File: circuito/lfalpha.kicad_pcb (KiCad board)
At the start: 2 copper layers, 200 x 100 mm, 48 parts, among them J1 BAT, J2 ANALOG, J3 MotorA, J4 MotorB, J5 Bluetooth, J6 REMOTE S/S, J7 SPI, J8 SENSOR CON, J9 SENSOR BAR, SW1 ON/OFF, SW2 START, SW3 STOP, U1 AruinoNano, U2 DRV8835-Carrier, U3 QRE1113, U4 QRE1113, U5 QRE1113, U6 QRE1113, U7 QRE1113, U8 QRE1113

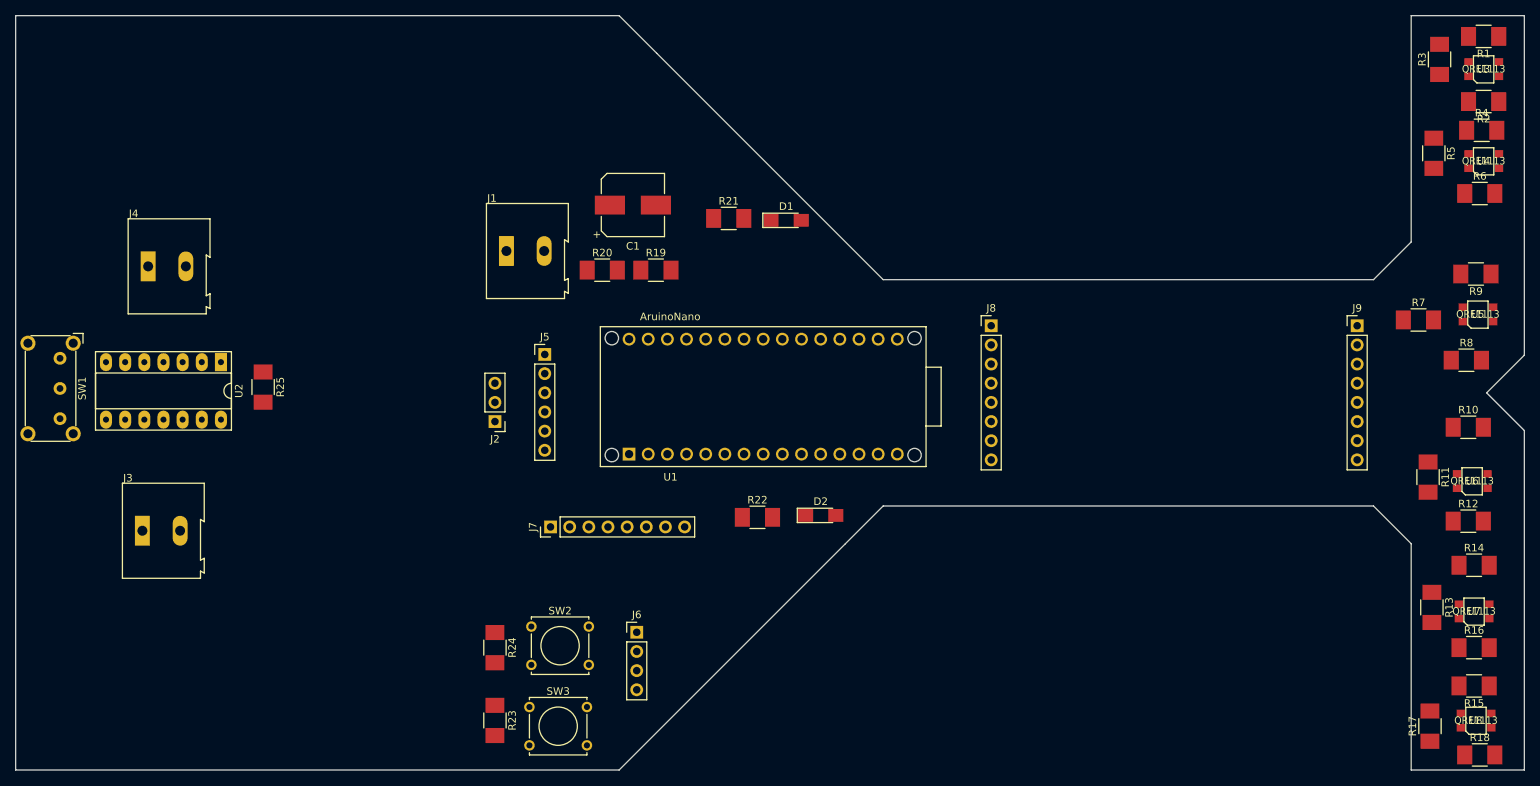
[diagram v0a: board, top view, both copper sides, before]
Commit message: Definito il layout del PCB definitivo
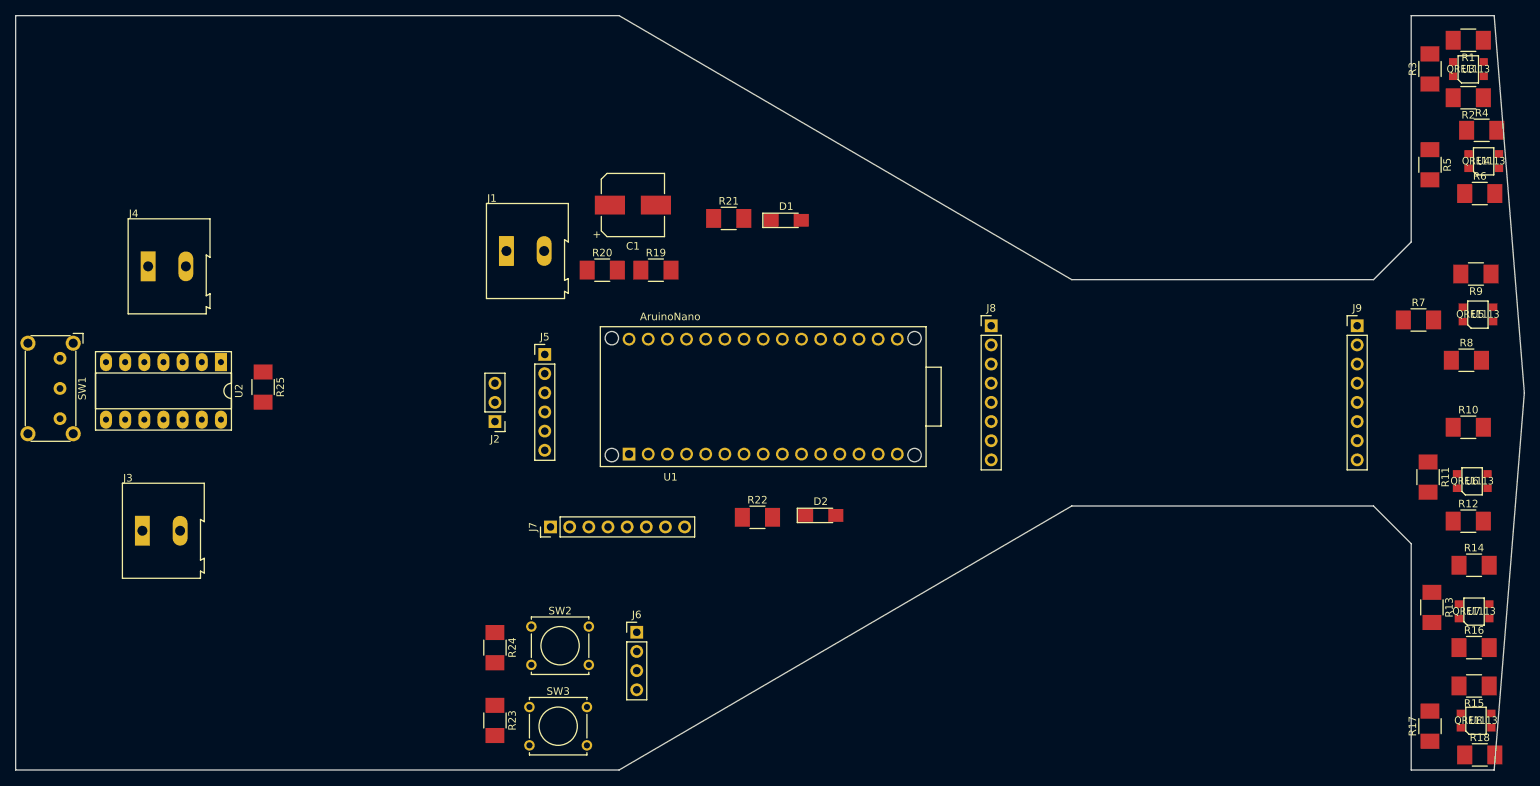
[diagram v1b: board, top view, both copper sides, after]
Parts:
- moved R1 2.09 mm to (242.6, 48.3)
- moved R2 2.09 mm to (242.6, 55.9)
- moved U3 2.03 mm to (242.6, 52.1)
- moved R3 1.80 mm to (237.5, 52.1)
- moved R5 1.61 mm to (237.5, 64.8)
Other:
- outline, holes or cut-outs redrawn
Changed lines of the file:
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@@
-(kicad_pcb (version 4) (host pcbnew 4.0.7-e0-6372~58~ubuntu14.04.1)
+(kicad_pcb (version 4) (host pcbnew 4.0.6)
   (general
     (links 125)
     (no_connects 125)
-    (area 40.455 44.377 250.075001 146.477)
+    (area 40.455 44.885 250.075001 146.477)
     (thickness 1.6)
-    (drawings 19)
+    (drawings 15)
     (tracks 0)
     (zones 0)
@@
   )
   (module QRE1113:4LEADSMD (layer F.Cu)
-    (at 244.602 52.07)
+    (at 242.57 52.07)
     (attr smd)
     (fp_text reference U3 (at 0 0) (layer F.SilkS)
@@
   )
   (module Resistors_SMD:R_1210_HandSoldering (layer F.Cu)
-    (at 244.602 47.752 180)
+    (at 242.57 48.26 180)
     (descr "Resistor SMD 1210, hand soldering")
     (tags "resistor 1210")
@@
   )
   (module Resistors_SMD:R_1210_HandSoldering (layer F.Cu)
-    (at 244.602 56.388 180)
+    (at 242.57 55.88 180)
     (descr "Resistor SMD 1210, hand soldering")
     (tags "resistor 1210")
@@
   )
   (module Resistors_SMD:R_1210_HandSoldering (layer F.Cu)
-    (at 238.76 50.8 90)
+    (at 237.49 52.07 90)
     (descr "Resistor SMD 1210, hand soldering")
     (tags "resistor 1210")
@@
   )
   (module Resistors_SMD:R_1210_HandSoldering (layer F.Cu)
-    (at 237.998 63.246 270)
+    (at 237.49 64.77 270)
     (descr "Resistor SMD 1210, hand soldering")
     (tags "resistor 1210")
@@
     )
   )
+  (gr_line (start 246 145) (end 250 95) (angle 90) (layer Edge.Cuts) (width 0.15))
+  (gr_line (start 235 145) (end 246 145) (angle 90) (layer Edge.Cuts) (width 0.15))
+  (gr_line (start 246 45) (end 250 95) (angle 90) (layer Edge.Cuts) (width 0.15))
+  (gr_line (start 235 45) (end 246 45) (angle 90) (layer Edge.Cuts) (width 0.15))
+  (gr_line (start 190 110) (end 130 145) (angle 90) (layer Edge.Cuts) (width 0.15))
+  (gr_line (start 230 110) (end 190 110) (angle 90) (layer Edge.Cuts) (width 0.15))
+  (gr_line (start 190 80) (end 130 45) (angle 90) (layer Edge.Cuts) (width 0.15))
+  (gr_line (start 230 80) (end 190 80) (angle 90) (layer Edge.Cuts) (width 0.15))
   (gr_line (start 130 45) (end 50 45) (angle 90) (layer Edge.Cuts) (width 0.15))
-  (gr_line (start 135 50) (end 130 45) (angle 90) (layer Edge.Cuts) (width 0.15))
-  (gr_line (start 165 80) (end 135 50) (angle 90) (layer Edge.Cuts) (width 0.15))
-  (gr_line (start 230 80) (end 165 80) (angle 90) (layer Edge.Cuts) (width 0.15))
   (gr_line (start 235 75) (end 230 80) (angle 90) (layer Edge.Cuts) (width 0.15))
   (gr_line (start 235 45) (end 235 75) (angle 90) (layer Edge.Cuts) (width 0.15))
-  (gr_line (start 250 45) (end 235 45) (angle 90) (layer Edge.Cuts) (width 0.15))
-  (gr_line (start 250 90) (end 250 45) (angle 90) (layer Edge.Cuts) (width 0.15))
-  (gr_line (start 245 95) (end 250 90) (angle 90) (layer Edge.Cuts) (width 0.15))
-  (gr_line (start 250 100) (end 245 95) (angle 90) (layer Edge.Cuts) (width 0.15))
-  (gr_line (start 250 145) (end 250 100) (angle 90) (layer Edge.Cuts) (width 0.15))
-  (gr_line (start 235 145) (end 250 145) (angle 90) (layer Edge.Cuts) (width 0.15))
   (gr_line (start 235 115) (end 235 145) (angle 90) (layer Edge.Cuts) (width 0.15))
   (gr_line (start 230 110) (end 235 115) (angle 90) (layer Edge.Cuts) (width 0.15))
-  (gr_line (start 165 110) (end 230 110) (angle 90) (layer Edge.Cuts) (width 0.15))
-  (gr_line (start 160 115) (end 165 110) (angle 90) (layer Edge.Cuts) (width 0.15))
-  (gr_line (start 130 145) (end 160 115) (angle 90) (layer Edge.Cuts) (width 0.15))
   (gr_line (start 50 145) (end 130 145) (angle 90) (layer Edge.Cuts) (width 0.15))
   (gr_line (start 50 45) (end 50 145) (angle 90) (layer Edge.Cuts) (width 0.15))

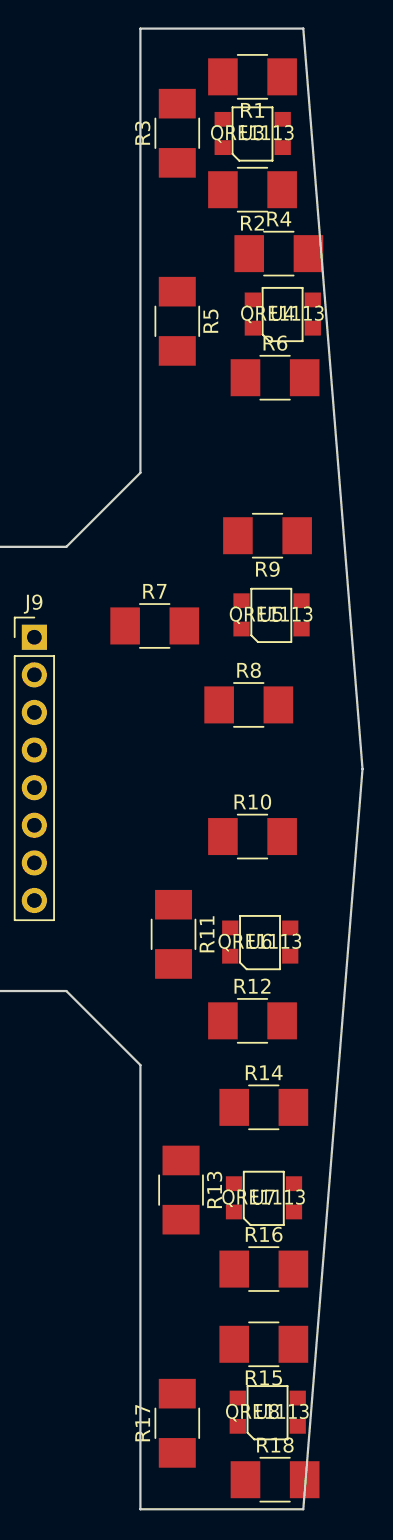
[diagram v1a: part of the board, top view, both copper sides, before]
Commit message: Disposti i componenti per la barra sensori
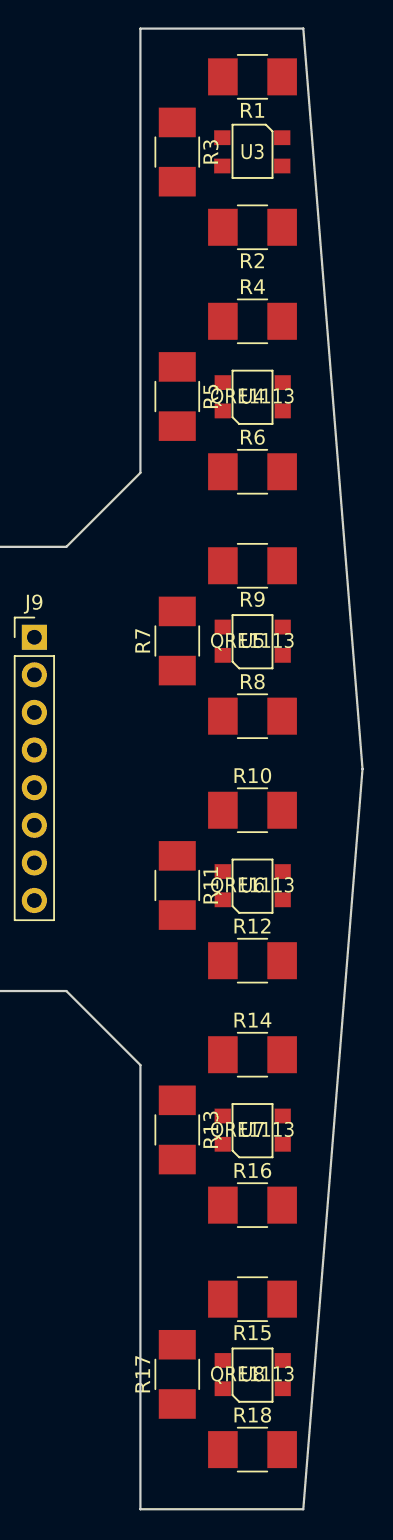
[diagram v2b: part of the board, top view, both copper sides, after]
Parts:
- moved R6 6.53 mm to (242.6, 74.9)
- moved U4 5.95 mm to (242.6, 69.8)
- moved R5 5.08 mm to (237.5, 69.8)
- moved R4 4.91 mm to (242.6, 64.8)
- moved U7 4.64 mm to (242.6, 119.4)
- moved R16 4.38 mm to (242.6, 124.5)
- moved R13 4.07 mm to (237.5, 119.4)
- moved R12 4.06 mm to (242.6, 108.0)
- moved U6 3.84 mm to (242.6, 102.9)
- moved R14 3.64 mm to (242.6, 114.3)
- moved R11 3.31 mm to (237.5, 102.9)
- moved R17 3.30 mm to (237.5, 135.9)
- moved R15 3.14 mm to (242.6, 130.8)
- moved U8 2.74 mm to (242.6, 135.9)
- moved R18 2.54 mm to (242.6, 141.0)
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
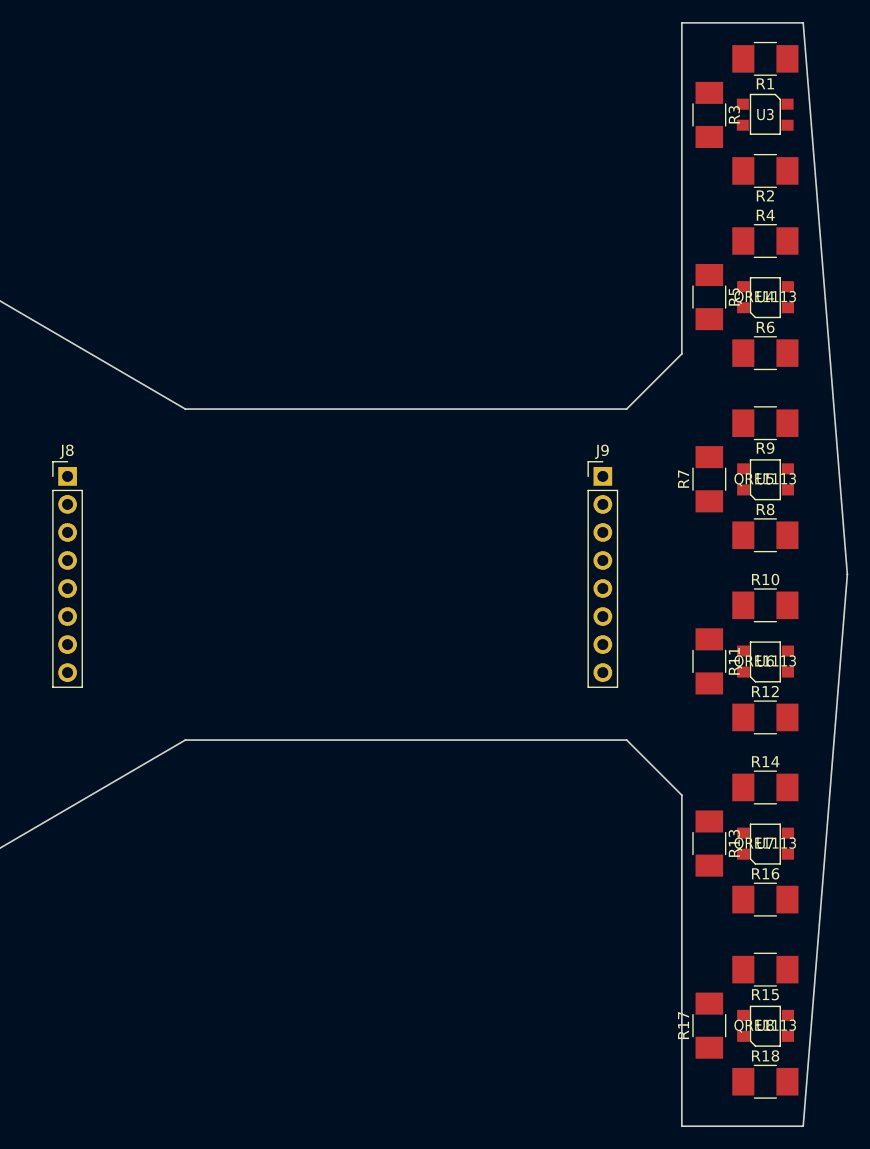
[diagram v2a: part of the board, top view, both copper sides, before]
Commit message: Sistemata la disposizione della barra sensori e completati i primi collegamenti, manca la parte relativa all'alimentazione
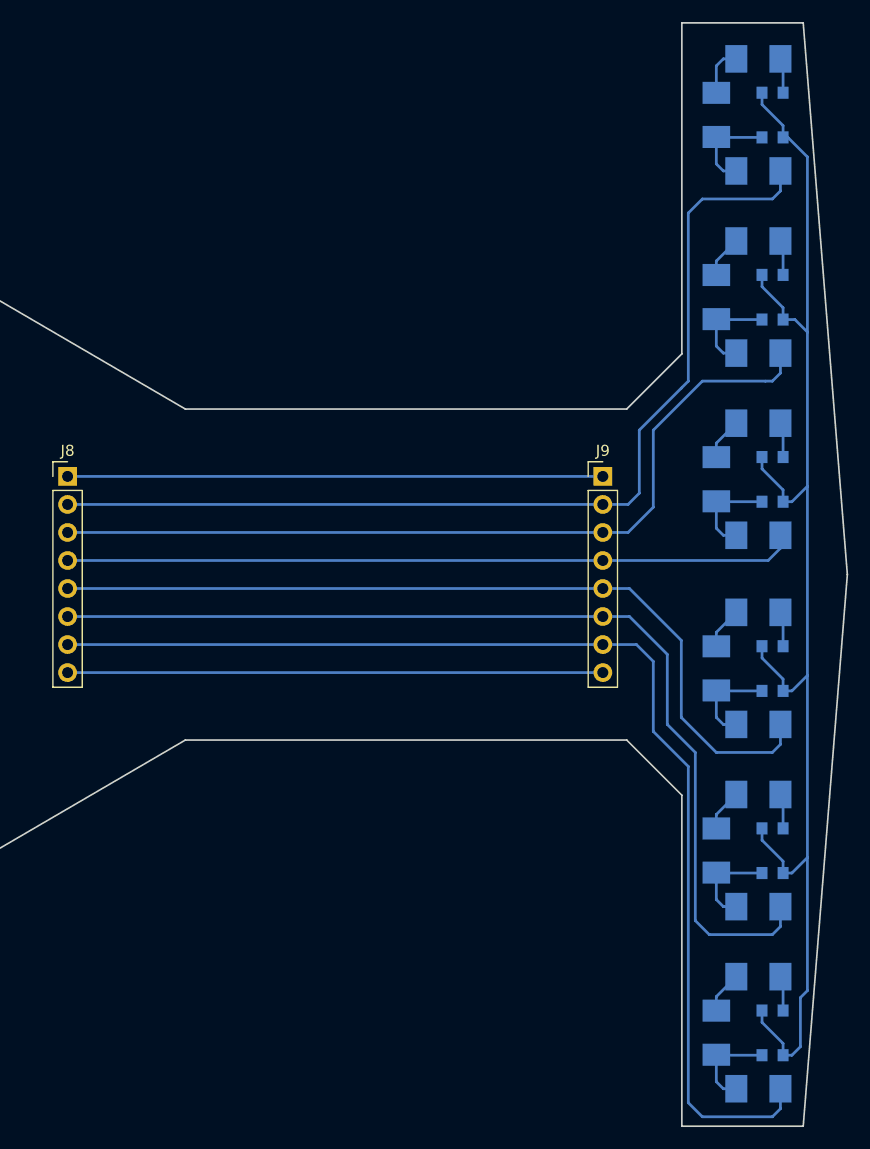
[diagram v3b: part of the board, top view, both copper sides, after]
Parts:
- R1, R10, R11, R12, R13, R14, R15, R16, R17, R18, R2, R3, R4, R5, R6, R7, R8, R9, U3, U4, U5, U6, U7, U8: moved to B.Cu
- moved R9 10.2 mm to (241.9, 91.4), turned to 0 degrees
- moved R14 7.24 mm to (238.1, 120.0), turned to 270 degrees
- moved R16 7.01 mm to (241.9, 131.4)
- moved R2 6.75 mm to (238.1, 53.3), turned to 270 degrees
- moved R3 6.75 mm to (241.9, 58.4), turned to 0 degrees
- moved R7 6.75 mm to (241.9, 81.3), turned to 0 degrees
- moved R8 6.75 mm to (238.1, 86.4), turned to 270 degrees
- moved R13 6.29 mm to (241.9, 114.9), turned to 0 degrees
- moved R15 5.75 mm to (241.9, 125.1), turned to 0 degrees
- moved U8 0.90 mm to (243.2, 136.5), turned to 270 degrees
- moved U7 0.90 mm to (243.2, 120.0), turned to 270 degrees
- moved R17 0.90 mm to (238.1, 136.5), turned to 270 degrees
- moved U6 0.90 mm to (243.2, 103.5), turned to 270 degrees
- moved R10 0.90 mm to (241.9, 98.4)
- moved R11 0.90 mm to (238.1, 103.5)
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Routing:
- net GND: track 0.00 -> 174.3 mm
- net Net-(J8-Pad7): track 0.00 -> 106.0 mm
- net Net-(J8-Pad6): track 0.00 -> 91.3 mm
- net Net-(J8-Pad2): track 0.00 -> 90.5 mm
- net Net-(J8-Pad5): track 0.00 -> 77.0 mm
- net Net-(J8-Pad3): track 0.00 -> 76.5 mm
- net +5V: track 0.00 -> 72.2 mm
- net Net-(J8-Pad4): track 0.00 -> 66.2 mm
- net Net-(R5-Pad2): track 0.00 -> 8.67 mm
- net Net-(R8-Pad2): track 0.00 -> 8.67 mm
- net Net-(R11-Pad2): track 0.00 -> 8.67 mm
- net Net-(R14-Pad2): track 0.00 -> 8.67 mm
- net Net-(R2-Pad2): track 0.00 -> 8.67 mm
- net Net-(R17-Pad2): track 0.00 -> 8.67 mm
- net Net-(R4-Pad2): track 0.00 -> 3.17 mm
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
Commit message: Avanzamento realizzazione PCB
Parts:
- moved J2 68.9 mm to (178.8, 76.7), turned to 270 degrees
- moved R21 55.8 mm to (153.4, 127.0), turned to 180 degrees
- moved D1 55.2 mm to (145.8, 127.0)
- moved J7 54.4 mm to (175.3, 109.7), turned to 270 degrees
- moved J5 21.5 mm to (128.5, 109.7), turned to 90 degrees
- moved U2 15.7 mm to (63.5, 98.6), turned to 90 degrees
- moved D2 14.9 mm to (145.8, 121.4)
- moved R19 11.4 mm to (146.3, 78.2)
- moved R22 11.1 mm to (153.4, 121.4), turned to 180 degrees
- moved R20 9.92 mm to (137.7, 78.2)
- moved J6 9.35 mm to (138.7, 119.9)
- moved J1 5.74 mm to (115.6, 70.5)
- moved R25 2.17 mm to (84.8, 95.0)
- moved SW1 1.02 mm to (56.9, 90.4)
- moved J8 0.36 mm to (179.1, 86.4)
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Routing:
- net +5V: track 72.2 -> 183.3 mm, vias 0 -> 6
- net Net-(J8-Pad7): track 106.0 -> 148.7 mm
- net Net-(J8-Pad6): track 91.3 -> 129.5 mm
- net Net-(J8-Pad5): track 77.0 -> 110.4 mm
- net Net-(J8-Pad4): track 66.2 -> 95.8 mm
- net Net-(J8-Pad3): track 76.5 -> 101.6 mm
- net GND: track 174.3 -> 197.7 mm, vias 0 -> 1
- net Net-(J8-Pad2): track 90.5 -> 111.8 mm

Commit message: Cambiati i parametri delle piste per le specifiche di osh park
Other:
- net class Default: clearance 0.2 -> 0.1524; trace_width 0.25 -> 0.1524; via_dia 0.6 -> 0.6858; via_drill 0.4 -> 0.3302
- rule trace_clearance: 0.2 -> 0.1524
- rule trace_min: 0.2 -> 0.1524
- rule via_min_drill: 0.3 -> 0.3302
- rule via_min_size: 0.4 -> 0.6858
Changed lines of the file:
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@@
-(kicad_pcb (version 4) (host pcbnew 4.0.7-e1-6374~58~ubuntu14.04.1)
+(kicad_pcb (version 4) (host pcbnew 4.0.6)
   (general
     (links 125)
     (no_connects 63)
-    (area 40.455 44.885 250.100001 145.075001)
+    (area 41.5186 44.924999 250.100001 145.075001)
     (thickness 1.6)
     (drawings 16)
@@
   )
   (setup
-    (last_trace_width 0.25)
-    (trace_clearance 0.2)
+    (last_trace_width 0.1524)
+    (trace_clearance 0.1524)
     (zone_clearance 0.508)
     (zone_45_only no)
-    (trace_min 0.2)
+    (trace_min 0.1524)
     (segment_width 0.2)
     (edge_width 0.15)
-    (via_size 0.6)
-    (via_drill 0.4)
-    (via_min_size 0.4)
-    (via_min_drill 0.3)
-    (uvia_size 0.3)
-    (uvia_drill 0.1)
+    (via_size 0.6858)
+    (via_drill 0.3302)
+    (via_min_size 0.6858)
+    (via_min_drill 0.3302)
+    (uvia_size 0.762)
+    (uvia_drill 0.508)
     (uvias_allowed no)
-    (uvia_min_size 0.2)
-    (uvia_min_drill 0.1)
+    (uvia_min_size 0)
+    (uvia_min_drill 0)
     (pcb_text_width 0.3)
     (pcb_text_size 1.5 1.5)
@@
   (net 53 "Net-(U2-Pad8)")
   (net_class Default "This is the default net class."
-    (clearance 0.2)
-    (trace_width 0.25)
-    (via_dia 0.6)
-    (via_drill 0.4)
-    (uvia_dia 0.3)
-    (uvia_drill 0.1)
+    (clearance 0.1524)
+    (trace_width 0.1524)
+    (via_dia 0.6858)
+    (via_drill 0.3302)
+    (uvia_dia 0.762)
+    (uvia_drill 0.508)
     (add_net +5V)
     (add_net +BATT)
